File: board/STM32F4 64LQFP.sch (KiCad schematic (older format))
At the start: 13 parts, among them P2 SWD, U1 STM32F40X_LQFP64, X2 8MHz 10ppm

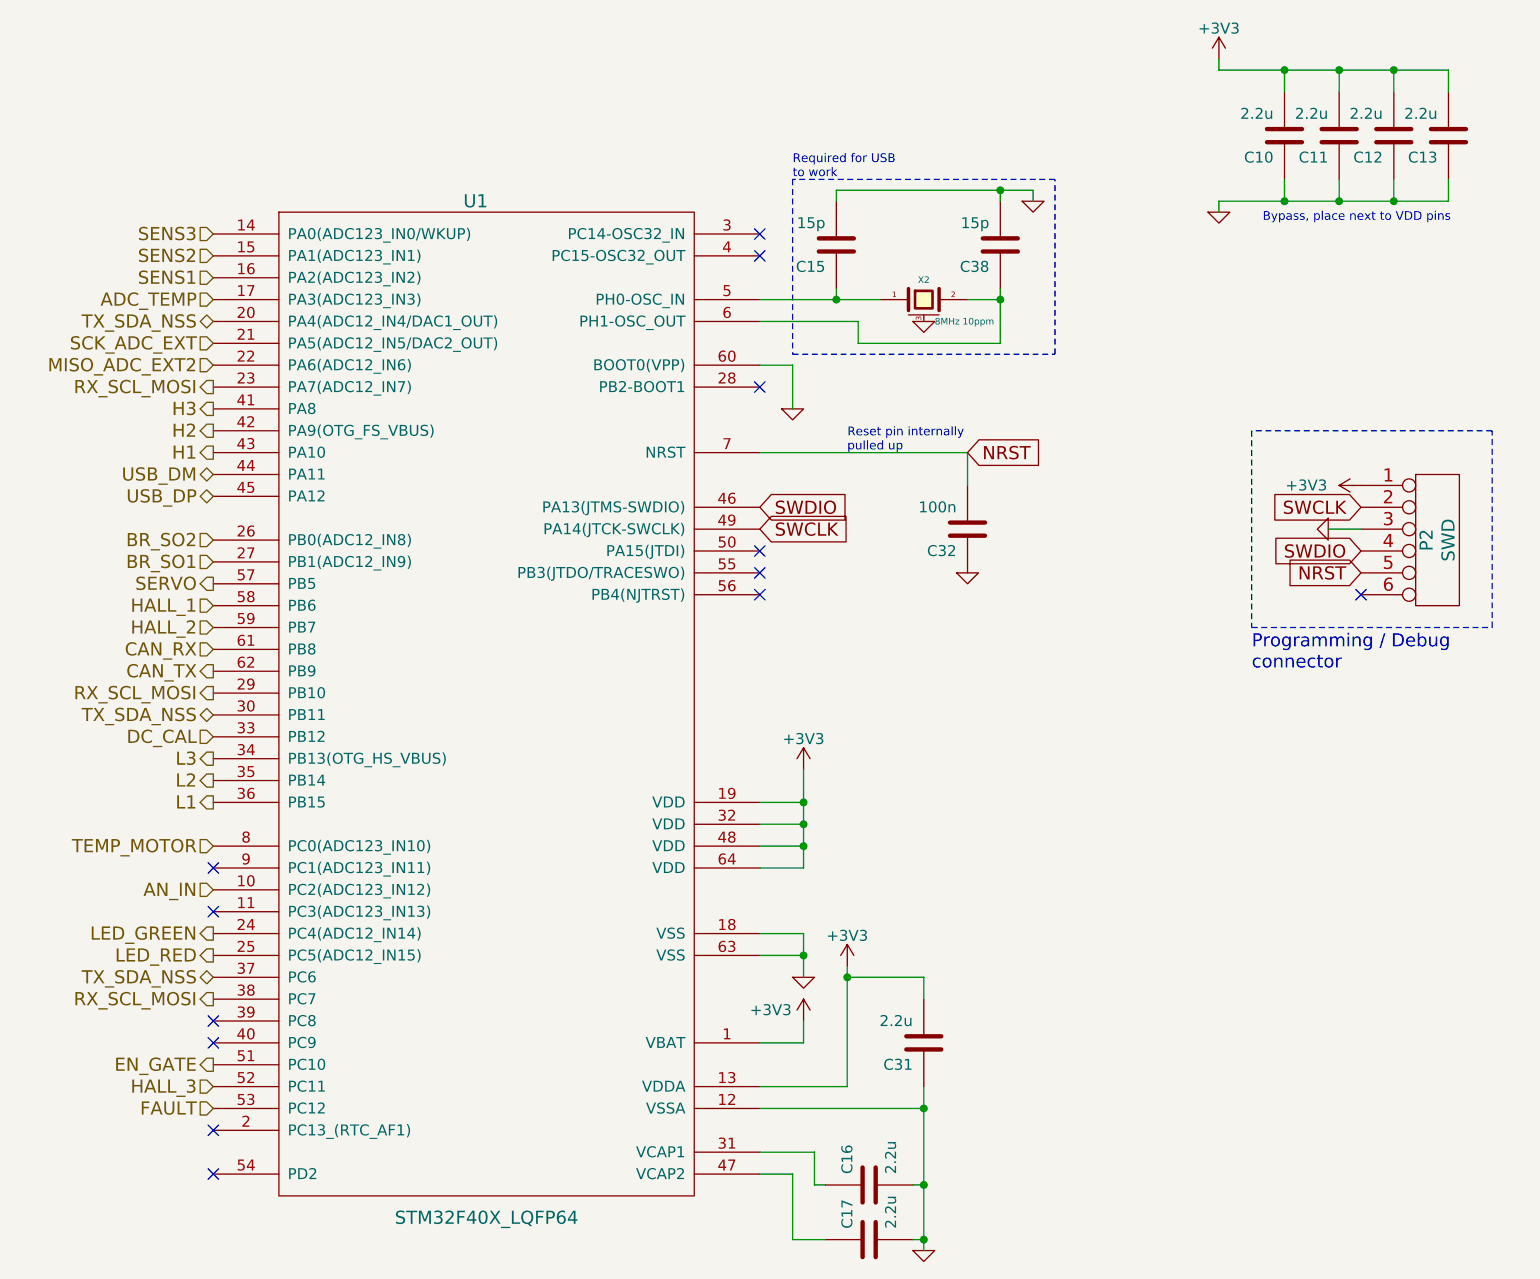
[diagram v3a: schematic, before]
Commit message: - updated layout with recent changes in schematic
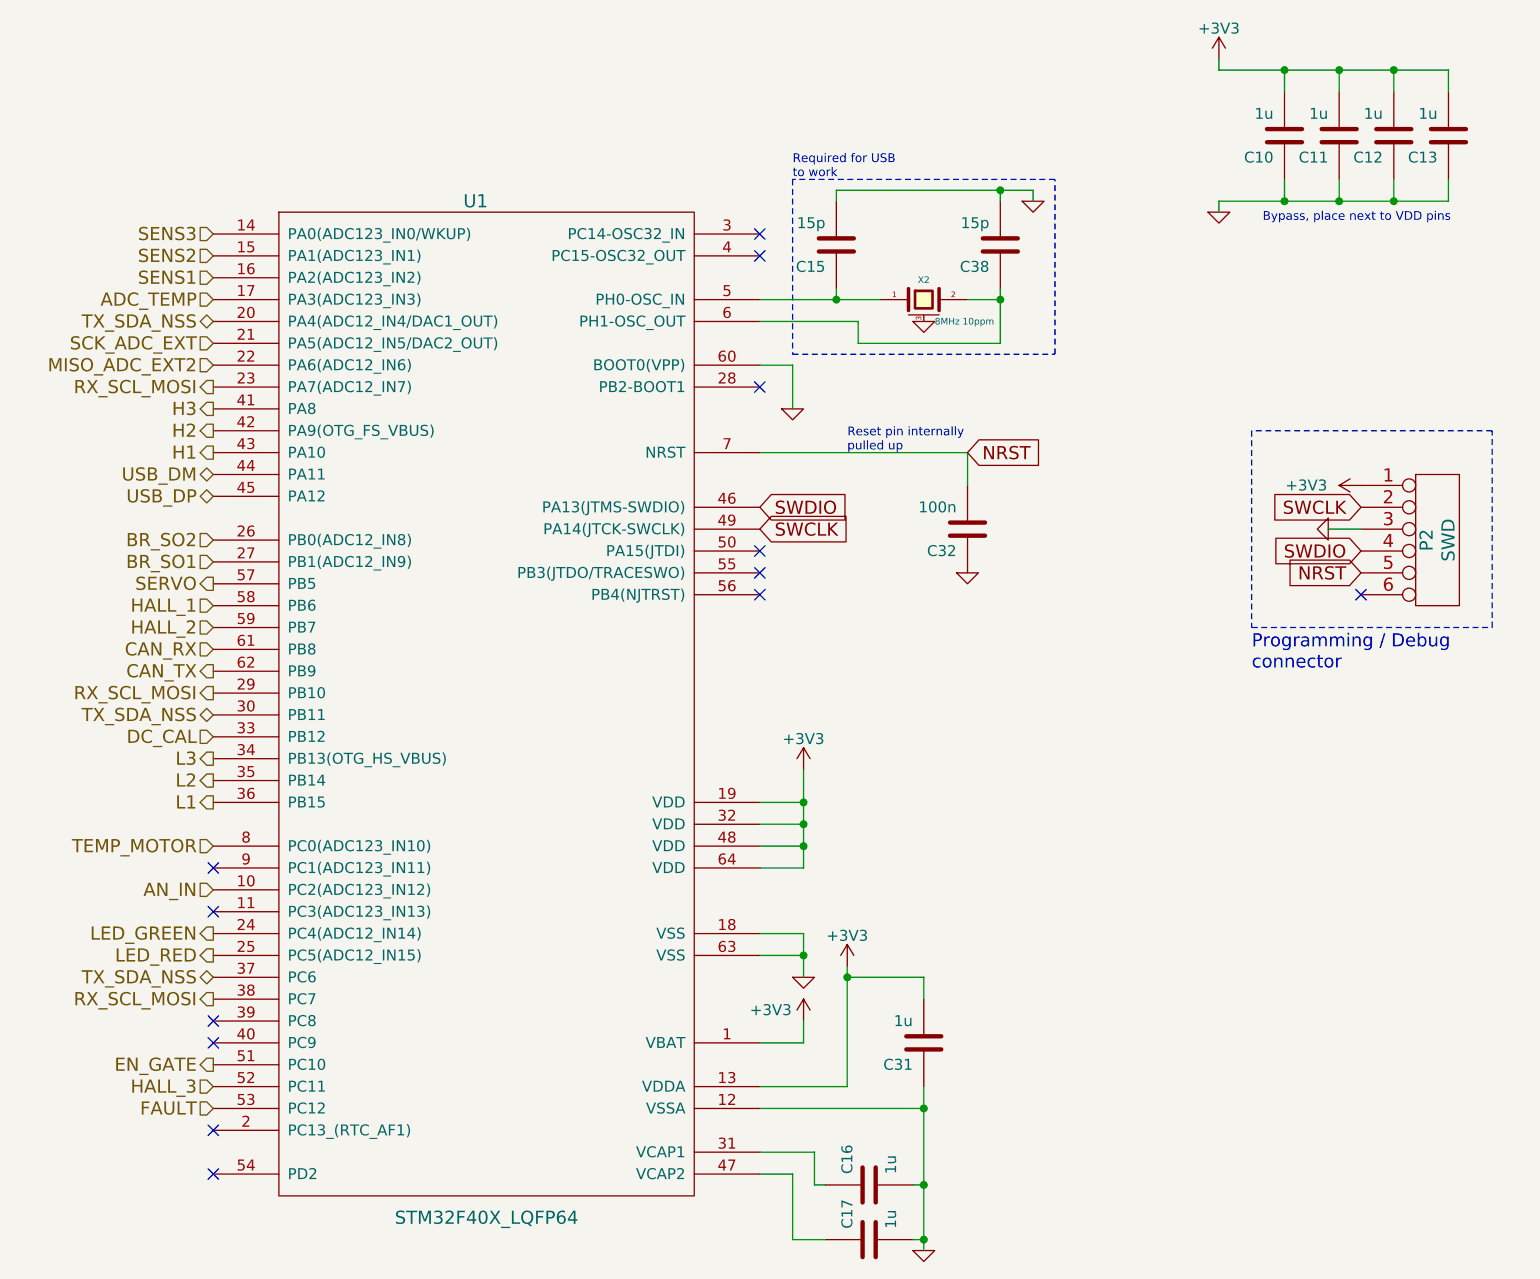
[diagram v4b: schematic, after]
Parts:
- C10, C11, C12, C13, C16, C17, C31: value 2.2u -> 1u
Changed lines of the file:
@@
 P 7500 6350
 F 0 "C17" H 7550 6450 50  0000 L CNN
-F 1 "2.2u" H 7550 6250 50  0000 L CNN
+F 1 "1u" H 7550 6250 50  0000 L CNN
 F 2 "Capacitors_SMD:C_0805" H 7500 6350 60  0001 C CNN
 F 3 "" H 7500 6350 60  0001 C CNN
@@
 P 7500 6100
 F 0 "C16" H 7550 6200 50  0000 L CNN
-F 1 "2.2u" H 7550 6000 50  0000 L CNN
+F 1 "1u" H 7550 6000 50  0000 L CNN
 F 2 "Capacitors_SMD:C_0805" H 7500 6100 60  0001 C CNN
 F 3 "" H 7500 6100 60  0001 C CNN
@@
 P 7750 5450
 F 0 "C31" H 7800 5550 50  0000 L CNN
-F 1 "2.2u" H 7800 5350 50  0000 L CNN
+F 1 "1u" H 7800 5350 50  0000 L CNN
 F 2 "Capacitors_SMD:C_0805" H 7750 5450 60  0001 C CNN
 F 3 "" H 7750 5450 60  0001 C CNN
@@
 P 9400 1300
 F 0 "C10" H 9450 1400 50  0000 L CNN
-F 1 "2.2u" H 9450 1200 50  0000 L CNN
+F 1 "1u" H 9450 1200 50  0000 L CNN
 F 2 "Capacitors_SMD:C_0805" H 9400 1300 60  0001 C CNN
 F 3 "" H 9400 1300 60  0001 C CNN
@@
 P 9650 1300
 F 0 "C11" H 9700 1400 50  0000 L CNN
-F 1 "2.2u" H 9700 1200 50  0000 L CNN
+F 1 "1u" H 9700 1200 50  0000 L CNN
 F 2 "Capacitors_SMD:C_0805" H 9650 1300 60  0001 C CNN
 F 3 "" H 9650 1300 60  0001 C CNN
@@
 P 9900 1300
 F 0 "C12" H 9950 1400 50  0000 L CNN
-F 1 "2.2u" H 9950 1200 50  0000 L CNN
+F 1 "1u" H 9950 1200 50  0000 L CNN
 F 2 "Capacitors_SMD:C_0805" H 9900 1300 60  0001 C CNN
 F 3 "" H 9900 1300 60  0001 C CNN
@@
 P 10150 1300
 F 0 "C13" H 10200 1400 50  0000 L CNN
-F 1 "2.2u" H 10200 1200 50  0000 L CNN
+F 1 "1u" H 10200 1200 50  0000 L CNN
 F 2 "Capacitors_SMD:C_0805" H 10150 1300 60  0001 C CNN
 F 3 "" H 10150 1300 60  0001 C CNN
@@
 00 00 00 50 18 A4 4F 00 00 00 40 61 90 3E 01 00 00 00 85 41 FA 04 00 00 00 14 06 E9 13 00 00 00
 50 18 A4 4F 00 00 00 40 61 90 3E 01 00 00 00 85 41 FA 04 00 00 00 14 F6 FF 00 CF 05 3E 3D 48 21
-47 45 00 00 00 00 49 45 4E 44 AE 42 60 82 AA
+47 45 00 00 00 00 49 45 4E 44 AE 42 60 82 0A
 EndData
 $EndBitmap
@@
 9D 20 C6 37 81 40 20 10 08 04 02 81 D0 4E 10 E3 9B 40 20 10 08 04 02 81 40 68 27 88 F1 4D 20 10
 08 04 02 81 40 20 B4 13 C4 F8 26 10 08 04 02 81 40 20 10 DA 89 FF 07 6E 76 4C 5E B7 9B F3 6C 00
-00 00 00 49 45 4E 44 AE 42 60 82 99
+00 00 00 49 45 4E 44 AE 42 60 82 1B
 EndData
 $EndBitmap
